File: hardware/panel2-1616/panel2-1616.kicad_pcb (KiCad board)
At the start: 2 copper layers, 56 x 38 mm, 56 parts, among them J1 Conn_01x02_Male, J2 Conn_01x08_Male, J3 Conn_01x02, J5 Conn_01x02_Male, J6 Conn_01x02_Male, J7 Conn_01x02_Male, U1 A7105-MODULE, U2 AIC1734-33GUTR, U3 ATtiny1616-M, U5 DRV8837DSGR, U6 DRV8837DSGR, U7 DRV8837DSGR

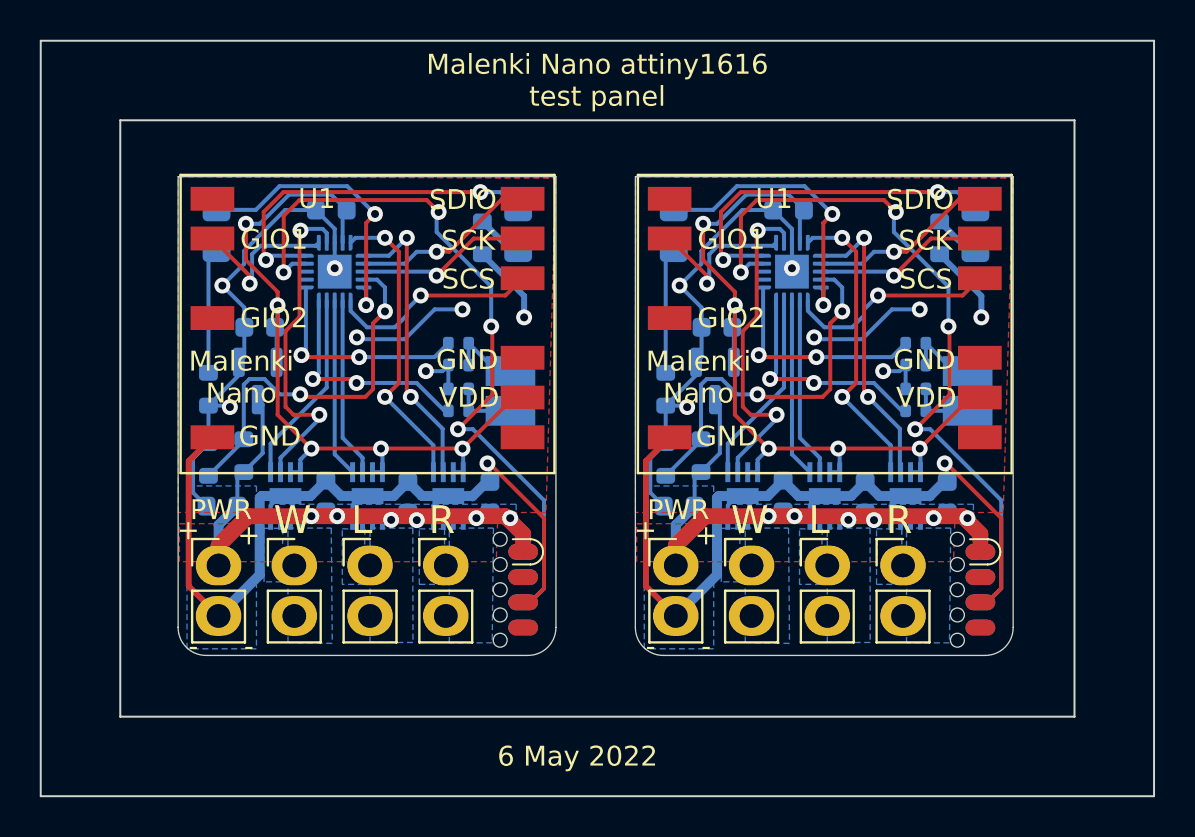
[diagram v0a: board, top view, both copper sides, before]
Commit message: Capacitor voltage rating
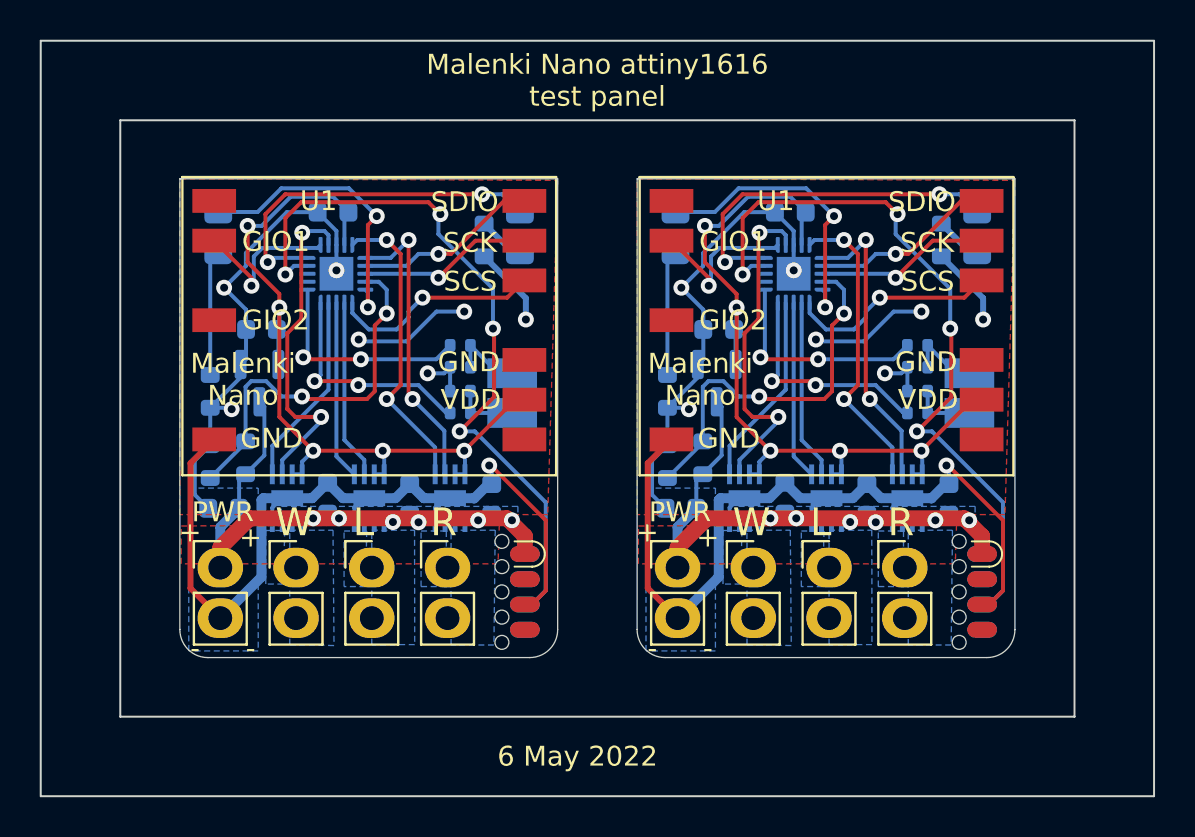
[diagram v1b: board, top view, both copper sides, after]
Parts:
- removed the C2 at (140.1, 110.4)
- removed the C2 at (117.1, 110.4)
- removed the C3 at (119.0, 101.4)
- removed the C3 at (142.0, 101.4)
- removed the C4 at (145.6, 95.5)
- removed the C4 at (122.6, 95.5)
- removed the C5 at (145.3, 109.9)
- removed the C5 at (122.3, 109.9)
- removed the C6 at (126.5, 110.0)
- removed the C6 at (149.5, 110.0)
- removed the C7 at (153.6, 110.0)
- removed the C7 at (130.6, 110.0)
- removed the D1 at (139.8, 96.5)
- removed the D1 at (116.8, 96.5)
- removed the D2 at (132.0, 96.5)
- removed the D2 at (155.0, 96.5)
- removed the J1 at (116.9, 113.4)
- removed the J1 at (139.9, 113.4)
- removed the J2 at (156.0, 114.6)
- removed the J2 at (133.0, 114.6)
- removed the J3 at (131.6, 104.6)
- removed the J3 at (154.6, 104.6)
- removed the J5 at (120.8, 113.4)
- removed the J5 at (143.8, 113.4)
- removed the J6 at (124.6, 113.4)
- removed the J6 at (147.6, 113.4)
- removed the J7 at (151.4, 113.4)
- removed the J7 at (128.4, 113.4)
- removed the R1 at (139.4, 104.5)
- removed the R1 at (116.4, 104.5)
- removed the R2 at (130.2, 96.9)
- removed the R2 at (153.2, 96.9)
- removed the R3 at (141.2, 107.9)
- removed the R3 at (118.2, 107.9)
- removed the R4 at (139.4, 108.1)
- removed the R4 at (116.4, 108.1)
- removed the R5 at (152.0, 105.6)
- removed the R5 at (129.0, 105.6)
- removed the R6 at (152.0, 102.2)
- removed the R6 at (129.0, 102.2)
- removed the R7 at (152.0, 104.5)
- removed the R7 at (129.0, 104.5)
- removed the R8 at (152.0, 103.3)
- removed the R8 at (129.0, 103.3)
- removed the U1 at (124.4, 100.9)
- removed the U1 at (147.4, 100.9)
- removed the U2 at (118.9, 104.1)
- removed the U2 at (141.9, 104.1)
- removed the U3 at (122.8, 98.6)
- removed the U3 at (145.8, 98.6)
- removed the U5 at (143.3, 109.9)
- removed the U5 at (120.3, 109.9)
- removed the U6 at (124.4, 109.9)
- removed the U6 at (147.4, 109.9)
- removed the U7 at (151.5, 109.9)
- removed the U7 at (128.5, 109.9)
- added C2: 10uF, Capacitor_SMD:C_0603_1608Metric, B.Cu at (117.2, 110.5)
- added C2: 10uF, Capacitor_SMD:C_0603_1608Metric, B.Cu at (140.2, 110.5)
- added C3: 10uF, Capacitor_SMD:C_0603_1608Metric, B.Cu at (119.1, 101.5)
- added C3: 10uF, Capacitor_SMD:C_0603_1608Metric, B.Cu at (142.1, 101.5)
- added C4: 0.1uF, Capacitor_SMD:C_0603_1608Metric, B.Cu at (145.7, 95.6)
- added C4: 0.1uF, Capacitor_SMD:C_0603_1608Metric, B.Cu at (122.7, 95.6)
- added C5: 10uF, Capacitor_SMD:C_0603_1608Metric, B.Cu at (145.4, 110.0)
- added C5: 10uF, Capacitor_SMD:C_0603_1608Metric, B.Cu at (122.4, 110.0)
- added C6: 10uF, Capacitor_SMD:C_0603_1608Metric, B.Cu at (149.6, 110.1)
- added C6: 10uF, Capacitor_SMD:C_0603_1608Metric, B.Cu at (126.6, 110.1)
- added C7: 10uF, Capacitor_SMD:C_0603_1608Metric, B.Cu at (130.7, 110.1)
- added C7: 10uF, Capacitor_SMD:C_0603_1608Metric, B.Cu at (153.7, 110.1)
- added D1: LED Blue, LED_SMD:LED_0805_2012Metric_Pad1.15x1.40mm_HandSolder, B.Cu at (139.9, 96.6)
- added D1: LED Blue, LED_SMD:LED_0805_2012Metric_Pad1.15x1.40mm_HandSolder, B.Cu at (116.9, 96.6)
- added D2: LED Red, LED_SMD:LED_0805_2012Metric_Pad1.15x1.40mm_HandSolder, B.Cu at (132.1, 96.6)
- added D2: LED Red, LED_SMD:LED_0805_2012Metric_Pad1.15x1.40mm_HandSolder, B.Cu at (155.1, 96.6)
- added J1: Conn_01x02_Male, malenki-nano:PinHeader_1x02_P2.54mm_BIG1, F.Cu at (117.0, 113.5)
- added J1: Conn_01x02_Male, malenki-nano:PinHeader_1x02_P2.54mm_BIG1, F.Cu at (140.0, 113.5)
- added J2: Conn_01x08_Male, malenki-nano:SOIC_clipProgSmall, F.Cu at (156.1, 114.7)
- added J2: Conn_01x08_Male, malenki-nano:SOIC_clipProgSmall, F.Cu at (133.1, 114.7)
- added J3: Conn_01x02, malenki-nano:wirepad_2, B.Cu at (131.7, 104.7)
- added J3: Conn_01x02, malenki-nano:wirepad_2, B.Cu at (154.7, 104.7)
- added J5: Conn_01x02_Male, malenki-nano:PinHeader_1x02_P2.54mm_BIG1, F.Cu at (143.8, 113.5)
- added J5: Conn_01x02_Male, malenki-nano:PinHeader_1x02_P2.54mm_BIG1, F.Cu at (120.8, 113.5)
- added J6: Conn_01x02_Male, malenki-nano:PinHeader_1x02_P2.54mm_BIG1, F.Cu at (147.7, 113.5)
- added J6: Conn_01x02_Male, malenki-nano:PinHeader_1x02_P2.54mm_BIG1, F.Cu at (124.7, 113.5)
- added J7: Conn_01x02_Male, malenki-nano:PinHeader_1x02_P2.54mm_BIG1, F.Cu at (128.5, 113.5)
- added J7: Conn_01x02_Male, malenki-nano:PinHeader_1x02_P2.54mm_BIG1, F.Cu at (151.5, 113.5)
- added R1: 220R, Resistor_SMD:R_0603_1608Metric, B.Cu at (116.5, 104.6)
- added R1: 220R, Resistor_SMD:R_0603_1608Metric, B.Cu at (139.5, 104.6)
- added R2: 220R, Resistor_SMD:R_0603_1608Metric, B.Cu at (153.3, 97.0)
- added R2: 220R, Resistor_SMD:R_0603_1608Metric, B.Cu at (130.3, 97.0)
- added R3: 33k, Resistor_SMD:R_0603_1608Metric, B.Cu at (141.3, 108.0)
- added R3: 33k, Resistor_SMD:R_0603_1608Metric, B.Cu at (118.3, 108.0)
- added R4: 10k, Resistor_SMD:R_0603_1608Metric, B.Cu at (139.5, 108.2)
- added R4: 10k, Resistor_SMD:R_0603_1608Metric, B.Cu at (116.5, 108.2)
- added R5: 470R, Resistor_SMD:R_0402_1005Metric, B.Cu at (152.1, 105.7)
- added R5: 470R, Resistor_SMD:R_0402_1005Metric, B.Cu at (129.1, 105.7)
- added R6: 470R, Resistor_SMD:R_0402_1005Metric, B.Cu at (129.1, 102.3)
- added R6: 470R, Resistor_SMD:R_0402_1005Metric, B.Cu at (152.1, 102.3)
- added R7: 10k, Resistor_SMD:R_0402_1005Metric, B.Cu at (129.1, 104.6)
- added R7: 10k, Resistor_SMD:R_0402_1005Metric, B.Cu at (152.1, 104.6)
- added R8: 10k, Resistor_SMD:R_0402_1005Metric, B.Cu at (152.1, 103.4)
- added R8: 10k, Resistor_SMD:R_0402_1005Metric, B.Cu at (129.1, 103.4)
- added U1: A7105-MODULE, malenki-nano:A7105-module, F.Cu at (124.5, 101.1)
- added U1: A7105-MODULE, malenki-nano:A7105-module, F.Cu at (147.5, 101.1)
- added U2: AIC1734-33GUTR, Package_TO_SOT_SMD:SOT-23, B.Cu at (119.0, 104.2)
- added U2: AIC1734-33GUTR, Package_TO_SOT_SMD:SOT-23, B.Cu at (142.0, 104.2)
- added U3: ATtiny1616-M, Package_DFN_QFN:VQFN-20-1EP_3x3mm_P0.4mm_EP1.7x1.7mm, B.Cu at (145.9, 98.7)
- added U3: ATtiny1616-M, Package_DFN_QFN:VQFN-20-1EP_3x3mm_P0.4mm_EP1.7x1.7mm, B.Cu at (122.9, 98.7)
- added U5: DRV8837DSGR, malenki-nano:WSON-8-1EP_2x2mm_P0.5mm_HAND1, B.Cu at (143.4, 110.0)
- added U5: DRV8837DSGR, malenki-nano:WSON-8-1EP_2x2mm_P0.5mm_HAND1, B.Cu at (120.4, 110.0)
- added U6: DRV8837DSGR, malenki-nano:WSON-8-1EP_2x2mm_P0.5mm_HAND1, B.Cu at (124.5, 110.0)
- added U6: DRV8837DSGR, malenki-nano:WSON-8-1EP_2x2mm_P0.5mm_HAND1, B.Cu at (147.5, 110.0)
- added U7: DRV8837DSGR, malenki-nano:WSON-8-1EP_2x2mm_P0.5mm_HAND1, B.Cu at (128.6, 110.0)
- added U7: DRV8837DSGR, malenki-nano:WSON-8-1EP_2x2mm_P0.5mm_HAND1, B.Cu at (151.6, 110.0)
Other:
- outline, holes or cut-outs redrawn
